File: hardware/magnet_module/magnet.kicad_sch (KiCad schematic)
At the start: 5 parts, among them U2 Leaf_Logo

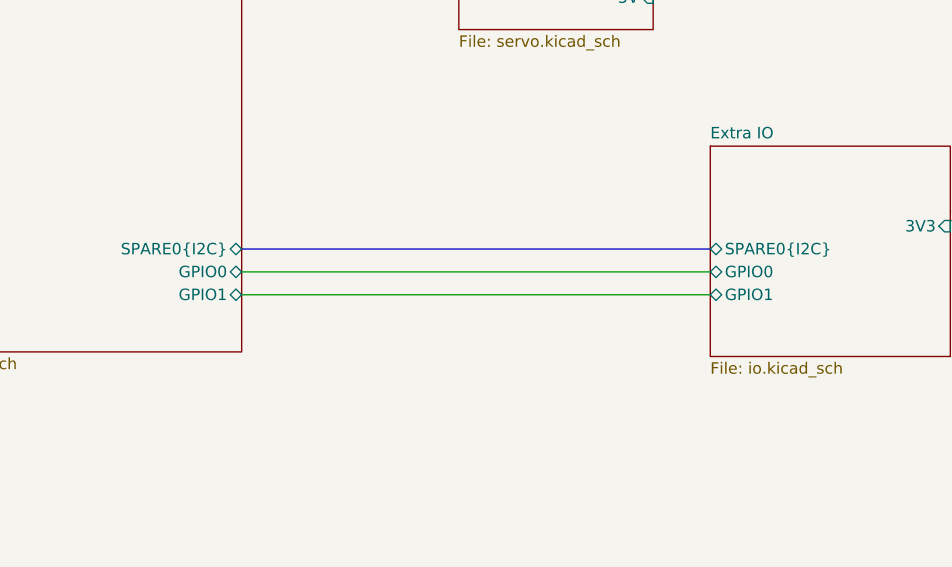
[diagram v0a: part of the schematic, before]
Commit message: Make schematic changes for the following v1.1 changes: * Add directional & latching connector to GPIO0 & GPIO1 * Add CAN IN / CAN OUT directionality * Add pulldown to BOOT pin and pullup to nRST * Correct servo orientation
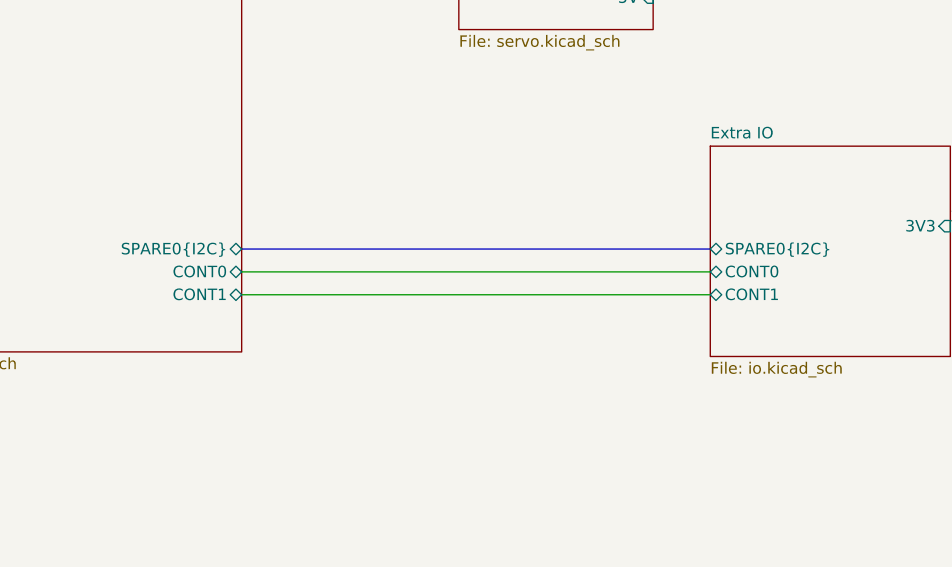
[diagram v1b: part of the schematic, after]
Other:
- sheet Extra IO ports: added CONT0, CONT1; removed GPIO0, GPIO1
- sheet MCU ports: added CONT0, CONT1; removed GPIO0, GPIO1
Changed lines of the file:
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@@
-			)
-		)
-		(pin "GPIO0" bidirectional
-			(at 168.91 123.19 0)
-			(effects
-				(font
-					(size 1.27 1.27)
-				)
-				(justify right)
-			)
-		)
-		(pin "GPIO1" bidirectional
-			(at 168.91 125.73 0)
-			(effects
-				(font
-					(size 1.27 1.27)
-				)
-				(justify right)
 			)
 		)
 		(pin "SERVO[0..1]" output
 			(at 168.91 91.44 0)
+			(effects
+				(font
+					(size 1.27 1.27)
+				)
+				(justify right)
+			)
+		)
+		(pin "CONT1" bidirectional
+			(at 168.91 125.73 0)
+			(effects
+				(font
+					(size 1.27 1.27)
+				)
+				(justify right)
+			)
+		)
+		(pin "CONT0" bidirectional
+			(at 168.91 123.19 0)
 			(effects
 				(font
@@
 			)
 		)
-		(pin "GPIO0" bidirectional
+		(pin "CONT1" bidirectional
+			(at 220.98 125.73 180)
+			(effects
+				(font
+					(size 1.27 1.27)
+				)
+				(justify left)
+			)
+		)
+		(pin "CONT0" bidirectional
 			(at 220.98 123.19 180)
 			(effects
 				(font
-					(size 1.27 1.27)
-				)
-				(justify left)
-			)
-		)
-		(pin "GPIO1" bidirectional
-			(at 220.98 125.73 180)
-			(effects
-				(font

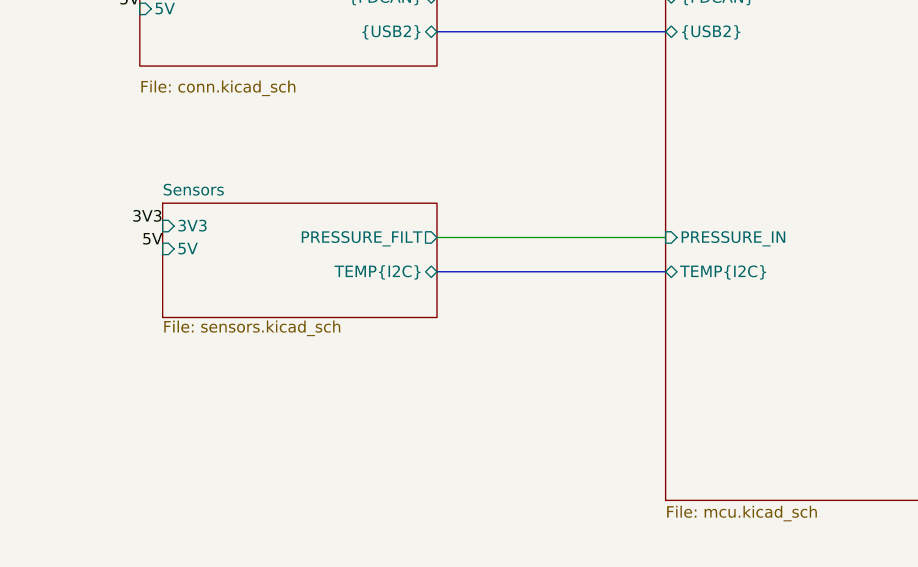
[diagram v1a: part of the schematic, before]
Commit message: add test points to schematic, generate step file including ultrasonic mic
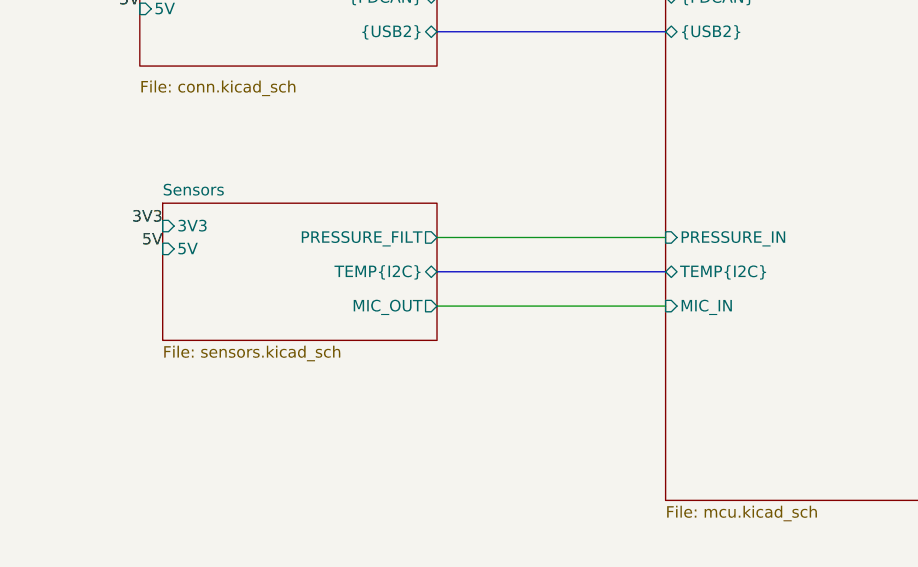
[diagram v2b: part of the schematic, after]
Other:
- sheet MCU ports: added MIC_IN; removed none
- sheet Sensors ports: added MIC_OUT; removed none
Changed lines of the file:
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@@
+		)
+	)
+	(wire
+		(pts
+			(xy 101.6 110.49) (xy 127 110.49)
+		)
+		(stroke
+			(width 0)
+			(type default)
 		)
 	)
@@
 			)
 		)
+		(pin "MIC_IN" input
+			(at 127 110.49 180)
+			(effects
+				(font
+					(size 1.27 1.27)
+				)
+				(justify left)
+			)
+		)
 		(instances
 			(project "magnet"
@@
 	(sheet
 		(at 71.12 99.06)
-		(size 30.48 12.7)
+		(size 30.48 15.24)
 		(fields_autoplaced yes)
 		(stroke
@@
 		)
 		(property "Sheetfile" "sensors.kicad_sch"
-			(at 71.12 112.0906 0)
+			(at 71.12 114.8846 0)
 			(effects
 				(font
@@
 			)
 		)
+		(pin "MIC_OUT" output
+			(at 101.6 110.49 0)
+			(effects
+				(font
+					(size 1.27 1.27)
+				)
+				(justify right)
+			)
+		)

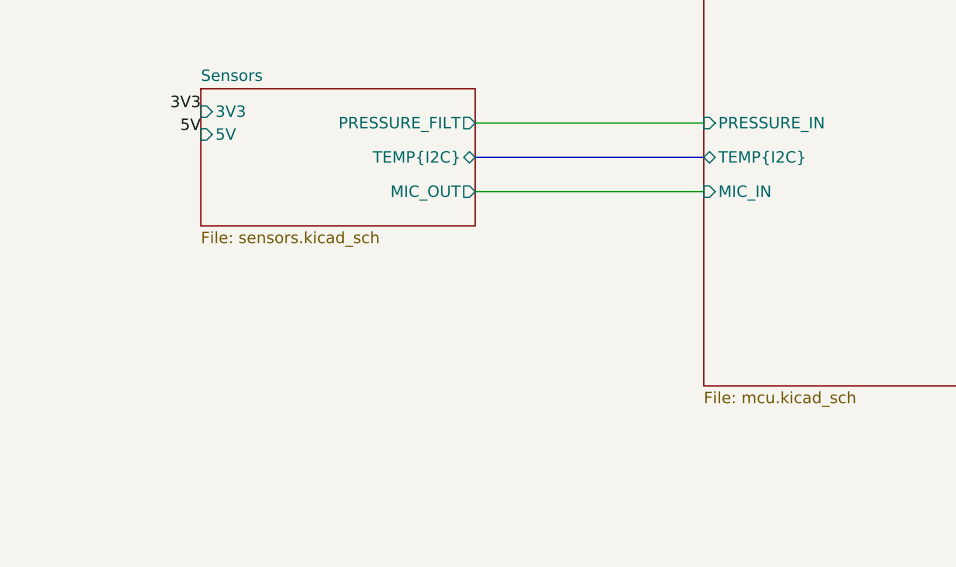
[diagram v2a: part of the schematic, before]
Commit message: Add ultrasonic microphone
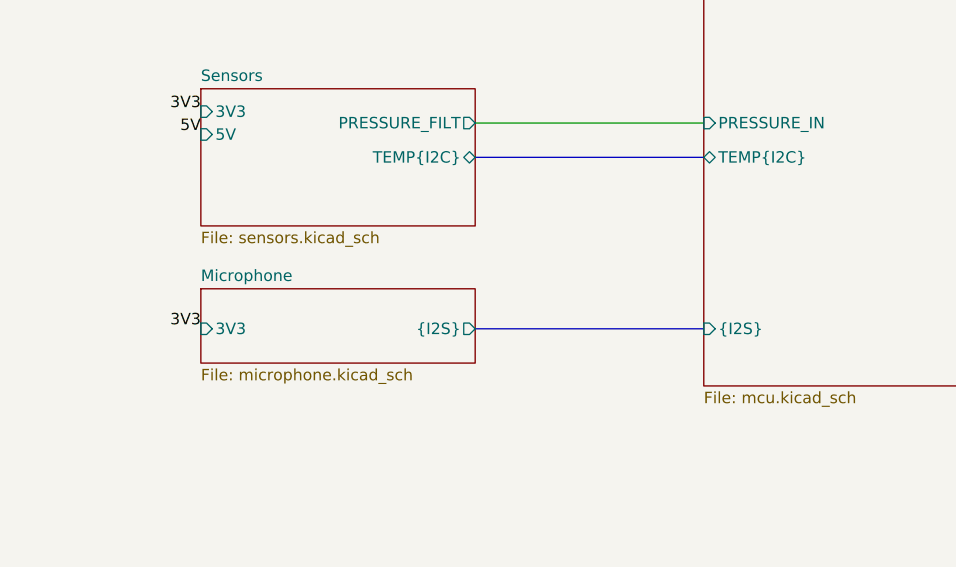
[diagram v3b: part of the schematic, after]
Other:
- added sheet Microphone (microphone.kicad_sch)
- sheet MCU ports: added {I2S}; removed MIC_IN
- sheet Sensors ports: added none; removed MIC_OUT
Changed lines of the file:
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@@
-		)
-	)
-	(wire
-		(pts
-			(xy 101.6 110.49) (xy 127 110.49)
-		)
-		(stroke
-			(width 0)
-			(type default)
 		)
 	)
@@
 		(pts
 			(xy 168.91 76.2) (xy 193.04 76.2)
+		)
+		(stroke
+			(width 0)
+			(type default)
+		)
+	)
+	(bus
+		(pts
+			(xy 101.6 125.73) (xy 127 125.73)
 		)
 		(stroke
@@
 			)
 			(justify left bottom)
+		)
+	)
+	(label "3V3"
+		(at 71.12 125.73 180)
+		(fields_autoplaced yes)
+		(effects
+			(font
+				(size 1.27 1.27)
+			)
+			(justify right bottom)
 		)
 	)
@@
 			)
 		)
-		(pin "MIC_IN" input
-			(at 127 110.49 180)
+		(pin "{I2S}" input
+			(at 127 125.73 180)
 			(effects
 				(font
@@
 	)
 	(sheet
+		(at 71.12 121.285)
+		(size 30.48 8.255)
+		(fields_autoplaced yes)
+		(stroke
+			(width 0.1524)
+			(type solid)
+		)
+		(fill
+			(color 0 0 0 0.0000)
+		)
+		(property "Sheetname" "Microphone"
+			(at 71.12 120.5734 0)
+			(effects
+				(font
+					(size 1.27 1.27)
+				)
+				(justify left bottom)
+			)
+		)
+		(property "Sheetfile" "microphone.kicad_sch"
+			(at 71.12 130.1246 0)
+			(effects
+				(font
+					(size 1.27 1.27)
+				)
+				(justify left top)
+			)
+		)
+		(pin "{I2S}" output
+			(at 101.6 125.73 0)
+			(effects
+				(font
+					(size 1.27 1.27)
+				)
+				(justify right)
+			)
+		)
+		(pin "3V3" input
+			(at 71.12 125.73 180)
+			(effects
+				(font
+					(size 1.27 1.27)
+				)
+				(justify left)
+			)
+		)
+		(instances
+			(project "magnet"
+				(path "/aa5044b8-67cd-4b5a-a593-0df9431eb095"
+					(page "9")
+				)
+			)
+		)
+	)
+	(sheet
 		(at 193.04 73.66)
 		(size 21.59 7.62)
@@
 			)
 		)
-		(pin "MIC_OUT" output
-			(at 101.6 110.49 0)
-			(effects
-				(font
-					(size 1.27 1.27)
-				)
-				(justify right)
-			)
-		)
